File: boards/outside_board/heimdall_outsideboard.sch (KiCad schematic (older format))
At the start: 6 parts

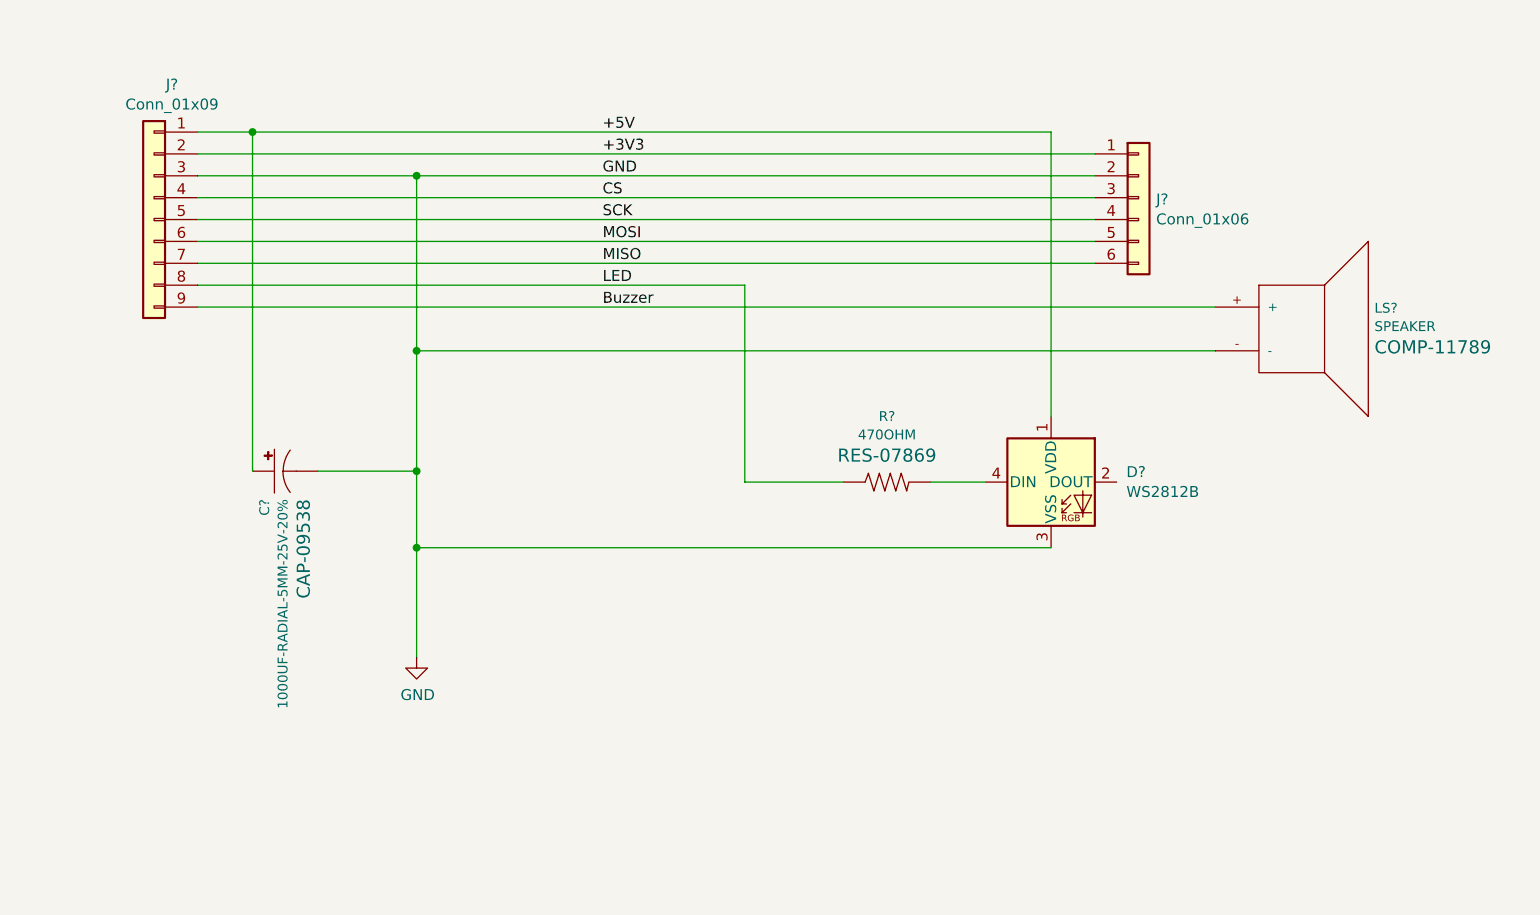
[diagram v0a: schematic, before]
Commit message: Annotate outside board, change paper layout and bump rev to 0.2.
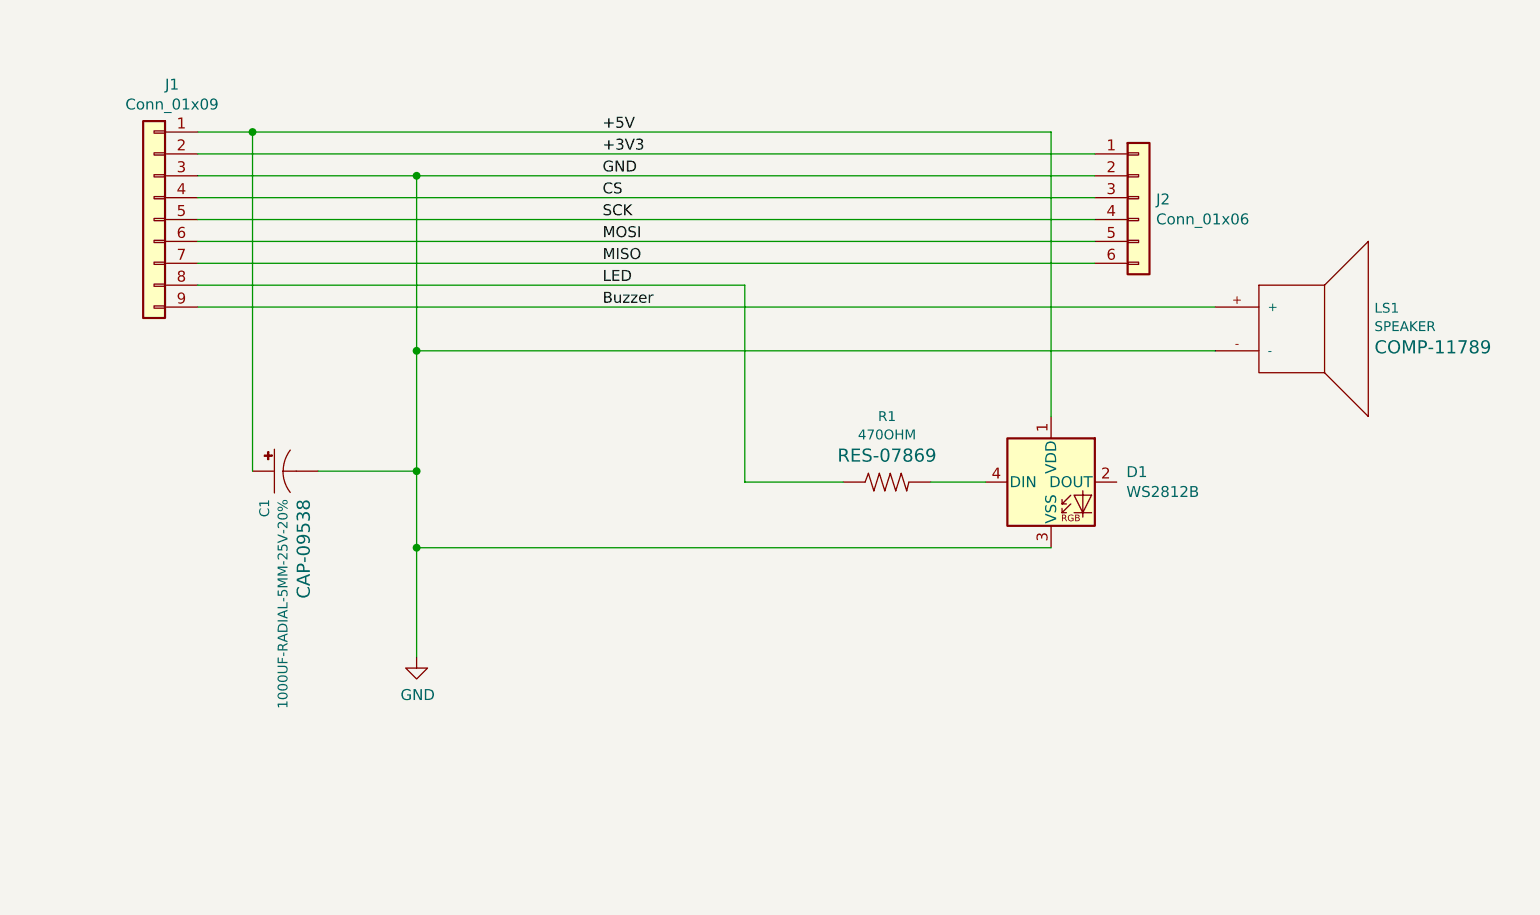
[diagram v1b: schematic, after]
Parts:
- gave numbers to parts that had none: 6
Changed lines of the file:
@@
 EELAYER 30 0
 EELAYER END
-$Descr A4 11693 8268
+$Descr USLetter 11000 8500
 encoding utf-8
 Sheet 1 1
 Title ""
 Date "2020-07-20"
-Rev "0.1"
+Rev "0.2"
 Comp ""
 Comment1 ""
@@
 $EndDescr
 $Comp
-L Connector_Generic:Conn_01x09 J?
+L Connector_Generic:Conn_01x09 J1
 U 1 1 5F14F04E
 P 1600 4050
-F 0 "J?" H 1518 4667 50  0000 C CNN
+F 0 "J1" H 1518 4667 50  0000 C CNN
 F 1 "Conn_01x09" H 1518 4576 50  0000 C CNN
 F 2 "" H 1600 4050 50  0001 C CNN
@@
 	1800 3850 2800 3850
 $Comp
-L power:GND #PWR?
+L power:GND #PWR01
 U 1 1 5F151F41
 P 2800 6050
-F 0 "#PWR?" H 2800 5800 50  0001 C CNN
+F 0 "#PWR01" H 2800 5800 50  0001 C CNN
 F 1 "GND" H 2805 5877 50  0000 C CNN
 F 2 "" H 2800 6050 50  0001 C CNN
@@
 $EndComp
 $Comp
-L SparkFun-Electromechanical:SPEAKER LS?
+L SparkFun-Electromechanical:SPEAKER LS1
 U 1 1 5F15A47C
 P 6850 4550
-F 0 "LS?" H 7178 4645 45  0000 L CNN
+F 0 "LS1" H 7178 4645 45  0000 L CNN
 F 1 "SPEAKER" H 7178 4561 45  0000 L CNN
 F 2 "PCB_MOUNT_SPEAKER" H 6850 4950 20  0001 C CNN
@@
 +5V
 $Comp
-L LED:WS2812B D?
+L LED:WS2812B D1
 U 1 1 5F15EA18
 P 5700 5250
-F 0 "D?" H 6044 5296 50  0000 L CNN
+F 0 "D1" H 6044 5296 50  0000 L CNN
 F 1 "WS2812B" H 6044 5205 50  0000 L CNN
 F 2 "LED_SMD:LED_WS2812B_PLCC4_5.0x5.0mm_P3.2mm" H 5750 4950 50  0001 L TNN
@@
 $EndComp
 $Comp
-L SparkFun-Resistors:470OHM R?
+L SparkFun-Resistors:470OHM R1
 U 1 1 5F162B61
 P 4950 5250
-F 0 "R?" H 4950 5550 45  0000 C CNN
+F 0 "R1" H 4950 5550 45  0000 C CNN
 F 1 "470OHM" H 4950 5466 45  0000 C CNN
 F 2 "0603" H 4950 5400 20  0001 C CNN
@@
 $EndComp
 $Comp
-L SparkFun-Capacitors:1000UF-RADIAL-5MM-25V-20% C?
+L SparkFun-Capacitors:1000UF-RADIAL-5MM-25V-20% C1
 U 1 1 5F15FBF3
 P 2150 5200
-F 0 "C?" H 2278 5245 45  0000 L CNN
+F 0 "C1" H 2278 5245 45  0000 L CNN
 F 1 "1000UF-RADIAL-5MM-25V-20%" H 2278 5161 45  0000 L CNN
 F 2 "CPOL-RADIAL-5MM-10MM" H 2150 5450 20  0001 C CNN
@@
 	1800 4250 5900 4250
 $Comp
-L Connector_Generic:Conn_01x06 J?
+L Connector_Generic:Conn_01x06 J2
 U 1 1 5F170A36
 P 6100 3950
-F 0 "J?" H 6180 3942 50  0000 L CNN
+F 0 "J2" H 6180 3942 50  0000 L CNN
 F 1 "Conn_01x06" H 6180 3851 50  0000 L CNN
 F 2 "" H 6100 3950 50  0001 C CNN

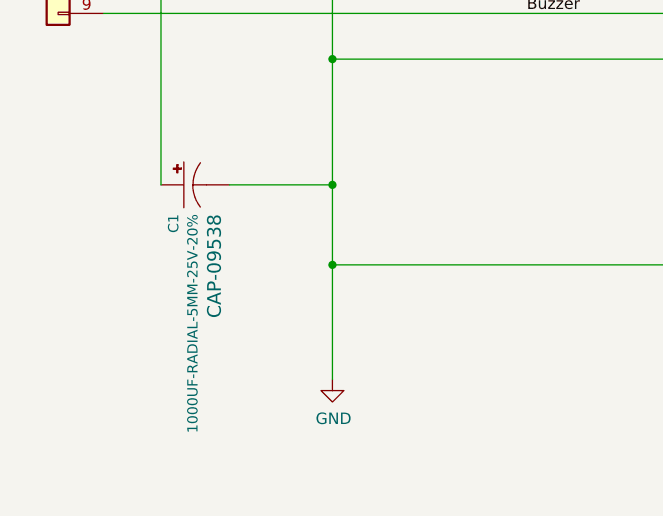
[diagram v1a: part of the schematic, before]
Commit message: Update outside board design with initial PCB layout
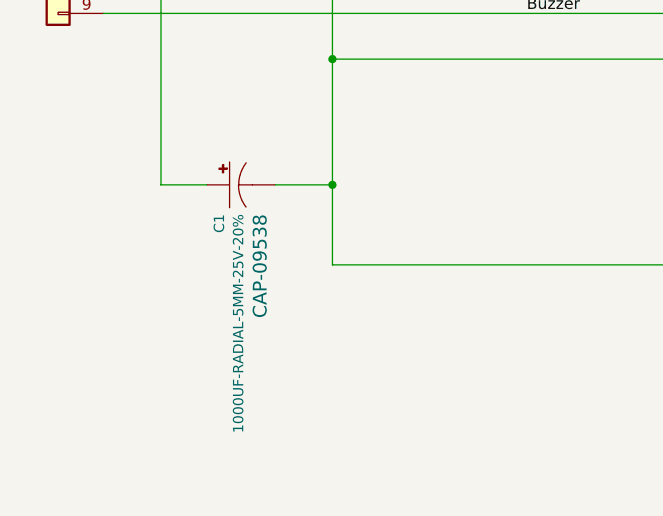
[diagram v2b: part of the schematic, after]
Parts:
- C1: footprint CPOL-RADIAL-5MM-10MM -> Capacitor_THT:CP_Radial_D12.5mm_P5.00mm
- J1: footprint (none) -> Connector_PinHeader_2.54mm:PinHeader_1x09_P2.54mm_Vertical
- J2: footprint (none) -> Connector_PinHeader_2.54mm:PinHeader_1x06_P2.54mm_Vertical
- LS1: footprint PCB_MOUNT_SPEAKER -> Electromechanical:PCB_MOUNT_SPEAKER
- R1: footprint 0603 -> Resistor_THT:R_Axial_DIN0918_L18.0mm_D9.0mm_P22.86mm_Horizontal
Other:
- moved on the sheet: C1
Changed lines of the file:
@@
 F 0 "J1" H 1518 4667 50  0000 C CNN
 F 1 "Conn_01x09" H 1518 4576 50  0000 C CNN
-F 2 "" H 1600 4050 50  0001 C CNN
+F 2 "Connector_PinHeader_2.54mm:PinHeader_1x09_P2.54mm_Vertical" H 1600 4050 50  0001 C CNN
 F 3 "~" H 1600 4050 50  0001 C CNN
 	1    1600 4050
@@
 	1800 3850 2800 3850
 $Comp
-L power:GND #PWR01
-U 1 1 5F151F41
-P 2800 6050
-F 0 "#PWR01" H 2800 5800 50  0001 C CNN
-F 1 "GND" H 2805 5877 50  0000 C CNN
-F 2 "" H 2800 6050 50  0001 C CNN
-F 3 "" H 2800 6050 50  0001 C CNN
-	1    2800 6050
-	1    0    0    -1
-$EndComp
-$Comp
 L SparkFun-Electromechanical:SPEAKER LS1
 U 1 1 5F15A47C
@@
 F 0 "LS1" H 7178 4645 45  0000 L CNN
 F 1 "SPEAKER" H 7178 4561 45  0000 L CNN
-F 2 "PCB_MOUNT_SPEAKER" H 6850 4950 20  0001 C CNN
+F 2 "Electromechanical:PCB_MOUNT_SPEAKER" H 6850 4950 20  0001 C CNN
 F 3 "" H 6850 4550 50  0001 C CNN
 F 4 "COMP-11789" H 7178 4466 60  0000 L CNN "Field4"
@@
 F 0 "R1" H 4950 5550 45  0000 C CNN
 F 1 "470OHM" H 4950 5466 45  0000 C CNN
-F 2 "0603" H 4950 5400 20  0001 C CNN
+F 2 "Resistor_THT:R_Axial_DIN0918_L18.0mm_D9.0mm_P22.86mm_Horizontal" H 4950 5400 20  0001 C CNN
 F 3 "" H 4950 5250 60  0001 C CNN
 F 4 "RES-07869" H 4950 5371 60  0000 C CNN "Field4"
@@
 L SparkFun-Capacitors:1000UF-RADIAL-5MM-25V-20% C1
 U 1 1 5F15FBF3
-P 2150 5200
-F 0 "C1" H 2278 5245 45  0000 L CNN
-F 1 "1000UF-RADIAL-5MM-25V-20%" H 2278 5161 45  0000 L CNN
-F 2 "CPOL-RADIAL-5MM-10MM" H 2150 5450 20  0001 C CNN
-F 3 "" H 2150 5200 50  0001 C CNN
-F 4 "CAP-09538" H 2278 5066 60  0000 L CNN "Field4"
-	1    2150 5200
+P 2350 5200
+F 0 "C1" H 2478 5245 45  0000 L CNN
+F 1 "1000UF-RADIAL-5MM-25V-20%" H 2478 5161 45  0000 L CNN
+F 2 "Capacitor_THT:CP_Radial_D12.5mm_P5.00mm" H 2350 5450 20  0001 C CNN
+F 3 "" H 2350 5200 50  0001 C CNN
+F 4 "CAP-09538" H 2478 5066 60  0000 L CNN "Field4"
+	1    2350 5200
 	0    -1   1    0
 $EndComp
@@
 F 0 "J2" H 6180 3942 50  0000 L CNN
 F 1 "Conn_01x06" H 6180 3851 50  0000 L CNN
-F 2 "" H 6100 3950 50  0001 C CNN
+F 2 "Connector_PinHeader_2.54mm:PinHeader_1x06_P2.54mm_Vertical" H 6100 3950 50  0001 C CNN
 F 3 "~" H 6100 3950 50  0001 C CNN
 	1    6100 3950
@@
 	5150 5250 5400 5250
 Wire Wire Line
-	2800 4650 2800 5200
-Wire Wire Line
 	2050 5200 2050 3650
 Connection ~ 2050 3650
 Wire Wire Line
-	2350 5200 2800 5200
-Connection ~ 2800 5200
-Wire Wire Line
-	2800 5200 2800 5550
-Wire Wire Line
 	5700 5550 2800 5550
-Connection ~ 2800 5550
-Wire Wire Line
-	2800 5550 2800 6050
 Wire Wire Line
 	5700 4950 5700 3650
 Wire Wire Line
 	2050 3650 5700 3650
+Wire Wire Line
+	2800 4650 2800 5200
+Wire Wire Line
+	2050 5200 2250 5200
+Wire Wire Line
+	2550 5200 2800 5200
+Connection ~ 2800 5200
+Wire Wire Line
+	2800 5200 2800 5550
 $EndSCHEMATC

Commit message: Outside board: replace the pin headers with screw terminals
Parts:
- removed J1: Conn_01x09, Connector_PinHeader_2.54mm:PinHeader_1x09_P2.54mm_Vertical, symbol Connector_Generic:Conn_01x09
- removed J2: Conn_01x06, Connector_PinHeader_2.54mm:PinHeader_1x06_P2.54mm_Vertical, symbol Connector_Generic:Conn_01x06
- added J1, J2, J3, J4, J5: Screw_Terminal_01x03, Connectors:SCREWTERMINAL-5MM-3, symbol Connector:Screw_Terminal_01x03
- C1: symbol SparkFun-Capacitors:1000UF-RADIAL-5MM-25V-20% -> heimdall_outsideboard-rescue:1000UF-RADIAL-5MM-25V-20%-SparkFun-Capacitors
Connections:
- net +3V3: now also J1.2 (Pin_2), J4.1 (Pin_1)
- net +5V: now also C1.1 (+), J1.1 (Pin_1); no longer C1.+
- net Buzzer: now also J3.3 (Pin_3)
- net CS: now also J2.1 (Pin_1), J4.3 (Pin_3)
- net GND: now also C1.2 (-), J1.3 (Pin_3), J4.2 (Pin_2); no longer C1.-
- net LED: now also J3.2 (Pin_2)
- net MISO: now also J3.1 (Pin_1), J5.3 (Pin_3)
- net MOSI: now also J2.3 (Pin_3), J5.2 (Pin_2)
- net SCK: now also J2.2 (Pin_2), J5.1 (Pin_1)
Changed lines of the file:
@@
 Comment4 ""
 $EndDescr
-$Comp
-L Connector_Generic:Conn_01x09 J1
-U 1 1 5F14F04E
-P 1600 4050
-F 0 "J1" H 1518 4667 50  0000 C CNN
-F 1 "Conn_01x09" H 1518 4576 50  0000 C CNN
-F 2 "Connector_PinHeader_2.54mm:PinHeader_1x09_P2.54mm_Vertical" H 1600 4050 50  0001 C CNN
-F 3 "~" H 1600 4050 50  0001 C CNN
-	1    1600 4050
-	-1   0    0    -1
-$EndComp
 Wire Wire Line
 	1800 3650 2050 3650
@@
 $EndComp
 $Comp
-L SparkFun-Capacitors:1000UF-RADIAL-5MM-25V-20% C1
+L heimdall_outsideboard-rescue:1000UF-RADIAL-5MM-25V-20%-SparkFun-Capacitors C1
 U 1 1 5F15FBF3
 P 2350 5200
@@
 Wire Wire Line
 	1800 4250 5900 4250
-$Comp
-L Connector_Generic:Conn_01x06 J2
-U 1 1 5F170A36
-P 6100 3950
-F 0 "J2" H 6180 3942 50  0000 L CNN
-F 1 "Conn_01x06" H 6180 3851 50  0000 L CNN
-F 2 "Connector_PinHeader_2.54mm:PinHeader_1x06_P2.54mm_Vertical" H 6100 3950 50  0001 C CNN
-F 3 "~" H 6100 3950 50  0001 C CNN
-	1    6100 3950
-	1    0    0    -1
-$EndComp
 Wire Wire Line
 	1800 4450 6450 4450
@@
 Wire Wire Line
 	2800 5200 2800 5550
+$Comp
+L Connector:Screw_Terminal_01x03 J1
+U 1 1 5F16624A
+P 1600 3750
+F 0 "J1" H 1518 4067 50  0000 C CNN
+F 1 "Screw_Terminal_01x03" H 1518 3976 50  0000 C CNN
+F 2 "Connectors:SCREWTERMINAL-5MM-3" H 1600 3750 50  0001 C CNN
+F 3 "~" H 1600 3750 50  0001 C CNN
+	1    1600 3750
+	-1   0    0    -1
+$EndComp
+$Comp
+L Connector:Screw_Terminal_01x03 J2
+U 1 1 5F166739
+P 1600 4050
+F 0 "J2" H 1518 4367 50  0000 C CNN
+F 1 "Screw_Terminal_01x03" H 1518 4276 50  0000 C CNN
+F 2 "Connectors:SCREWTERMINAL-5MM-3" H 1600 4050 50  0001 C CNN
+F 3 "~" H 1600 4050 50  0001 C CNN
+	1    1600 4050
+	-1   0    0    -1
+$EndComp
+$Comp
+L Connector:Screw_Terminal_01x03 J3
+U 1 1 5F166DE5
+P 1600 4350
+F 0 "J3" H 1518 4667 50  0000 C CNN
+F 1 "Screw_Terminal_01x03" H 1518 4576 50  0000 C CNN
+F 2 "Connectors:SCREWTERMINAL-5MM-3" H 1600 4350 50  0001 C CNN
+F 3 "~" H 1600 4350 50  0001 C CNN
+	1    1600 4350
+	-1   0    0    -1
+$EndComp
+$Comp
+L Connector:Screw_Terminal_01x03 J4
+U 1 1 5F1677E6
+P 6100 3850
+F 0 "J4" H 6180 3892 50  0000 L CNN
+F 1 "Screw_Terminal_01x03" H 6180 3801 50  0000 L CNN
+F 2 "Connectors:SCREWTERMINAL-5MM-3" H 6100 3850 50  0001 C CNN
+F 3 "~" H 6100 3850 50  0001 C CNN
+	1    6100 3850
+	1    0    0    -1
+$EndComp
+$Comp
+L Connector:Screw_Terminal_01x03 J5
+U 1 1 5F168062
+P 6100 4150
+F 0 "J5" H 6180 4192 50  0000 L CNN
+F 1 "Screw_Terminal_01x03" H 6180 4101 50  0000 L CNN
+F 2 "Connectors:SCREWTERMINAL-5MM-3" H 6100 4150 50  0001 C CNN
+F 3 "~" H 6100 4150 50  0001 C CNN
+	1    6100 4150
+	1    0    0    -1
+$EndComp
 $EndSCHEMATC

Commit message: Revert "Outside board: replace the pin headers with screw terminals"
This reverts commit 695c30ad44e01b6420bbd27eb88eba567c36bb63.
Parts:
- removed J1, J2, J3, J4, J5: Screw_Terminal_01x03, Connectors:SCREWTERMINAL-5MM-3, symbol Connector:Screw_Terminal_01x03
- added J1: Conn_01x09, Connector_PinHeader_2.54mm:PinHeader_1x09_P2.54mm_Vertical, symbol Connector_Generic:Conn_01x09
- added J2: Conn_01x06, Connector_PinHeader_2.54mm:PinHeader_1x06_P2.54mm_Vertical, symbol Connector_Generic:Conn_01x06
- C1: symbol heimdall_outsideboard-rescue:1000UF-RADIAL-5MM-25V-20%-SparkFun-Capacitors -> SparkFun-Capacitors:1000UF-RADIAL-5MM-25V-20%
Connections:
- net +3V3: now also J1.2 (Pin_2), J2.1 (Pin_1)
- net +5V: now also C1.+, J1.1 (Pin_1); no longer C1.1 (+)
- net Buzzer: now also J1.9 (Pin_9)
- net CS: now also J1.4 (Pin_4), J2.3 (Pin_3)
- net GND: now also C1.-, J1.3 (Pin_3), J2.2 (Pin_2); no longer C1.2 (-)
- net LED: now also J1.8 (Pin_8)
- net MISO: now also J1.7 (Pin_7), J2.6 (Pin_6)
- net MOSI: now also J1.6 (Pin_6), J2.5 (Pin_5)
- net SCK: now also J1.5 (Pin_5), J2.4 (Pin_4)
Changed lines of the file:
@@
 Comment4 ""
 $EndDescr
+$Comp
+L Connector_Generic:Conn_01x09 J1
+U 1 1 5F14F04E
+P 1600 4050
+F 0 "J1" H 1518 4667 50  0000 C CNN
+F 1 "Conn_01x09" H 1518 4576 50  0000 C CNN
+F 2 "Connector_PinHeader_2.54mm:PinHeader_1x09_P2.54mm_Vertical" H 1600 4050 50  0001 C CNN
+F 3 "~" H 1600 4050 50  0001 C CNN
+	1    1600 4050
+	-1   0    0    -1
+$EndComp
 Wire Wire Line
 	1800 3650 2050 3650
@@
 $EndComp
 $Comp
-L heimdall_outsideboard-rescue:1000UF-RADIAL-5MM-25V-20%-SparkFun-Capacitors C1
+L SparkFun-Capacitors:1000UF-RADIAL-5MM-25V-20% C1
 U 1 1 5F15FBF3
 P 2350 5200
@@
 Wire Wire Line
 	1800 4250 5900 4250
+$Comp
+L Connector_Generic:Conn_01x06 J2
+U 1 1 5F170A36
+P 6100 3950
+F 0 "J2" H 6180 3942 50  0000 L CNN
+F 1 "Conn_01x06" H 6180 3851 50  0000 L CNN
+F 2 "Connector_PinHeader_2.54mm:PinHeader_1x06_P2.54mm_Vertical" H 6100 3950 50  0001 C CNN
+F 3 "~" H 6100 3950 50  0001 C CNN
+	1    6100 3950
+	1    0    0    -1
+$EndComp
 Wire Wire Line
 	1800 4450 6450 4450
@@
 Wire Wire Line
 	2800 5200 2800 5550
-$Comp
-L Connector:Screw_Terminal_01x03 J1
-U 1 1 5F16624A
-P 1600 3750
-F 0 "J1" H 1518 4067 50  0000 C CNN
-F 1 "Screw_Terminal_01x03" H 1518 3976 50  0000 C CNN
-F 2 "Connectors:SCREWTERMINAL-5MM-3" H 1600 3750 50  0001 C CNN
-F 3 "~" H 1600 3750 50  0001 C CNN
-	1    1600 3750
-	-1   0    0    -1
-$EndComp
-$Comp
-L Connector:Screw_Terminal_01x03 J2
-U 1 1 5F166739
-P 1600 4050
-F 0 "J2" H 1518 4367 50  0000 C CNN
-F 1 "Screw_Terminal_01x03" H 1518 4276 50  0000 C CNN
-F 2 "Connectors:SCREWTERMINAL-5MM-3" H 1600 4050 50  0001 C CNN
-F 3 "~" H 1600 4050 50  0001 C CNN
-	1    1600 4050
-	-1   0    0    -1
-$EndComp
-$Comp
-L Connector:Screw_Terminal_01x03 J3
-U 1 1 5F166DE5
-P 1600 4350
-F 0 "J3" H 1518 4667 50  0000 C CNN
-F 1 "Screw_Terminal_01x03" H 1518 4576 50  0000 C CNN
-F 2 "Connectors:SCREWTERMINAL-5MM-3" H 1600 4350 50  0001 C CNN
-F 3 "~" H 1600 4350 50  0001 C CNN
-	1    1600 4350
-	-1   0    0    -1
-$EndComp
-$Comp
-L Connector:Screw_Terminal_01x03 J4
-U 1 1 5F1677E6
-P 6100 3850
-F 0 "J4" H 6180 3892 50  0000 L CNN
-F 1 "Screw_Terminal_01x03" H 6180 3801 50  0000 L CNN
-F 2 "Connectors:SCREWTERMINAL-5MM-3" H 6100 3850 50  0001 C CNN
-F 3 "~" H 6100 3850 50  0001 C CNN
-	1    6100 3850
-	1    0    0    -1
-$EndComp
-$Comp
-L Connector:Screw_Terminal_01x03 J5
-U 1 1 5F168062
-P 6100 4150
-F 0 "J5" H 6180 4192 50  0000 L CNN
-F 1 "Screw_Terminal_01x03" H 6180 4101 50  0000 L CNN
-F 2 "Connectors:SCREWTERMINAL-5MM-3" H 6100 4150 50  0001 C CNN
-F 3 "~" H 6100 4150 50  0001 C CNN
-	1    6100 4150
-	1    0    0    -1
-$EndComp
 $EndSCHEMATC
